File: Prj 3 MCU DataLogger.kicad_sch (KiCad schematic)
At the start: 25 parts, among them U1 24LC1025, U2 24LC1025, U3 DS1337S_, U4 ATMEGA328P-AU, Y1 Crystal, Y2 Crystal

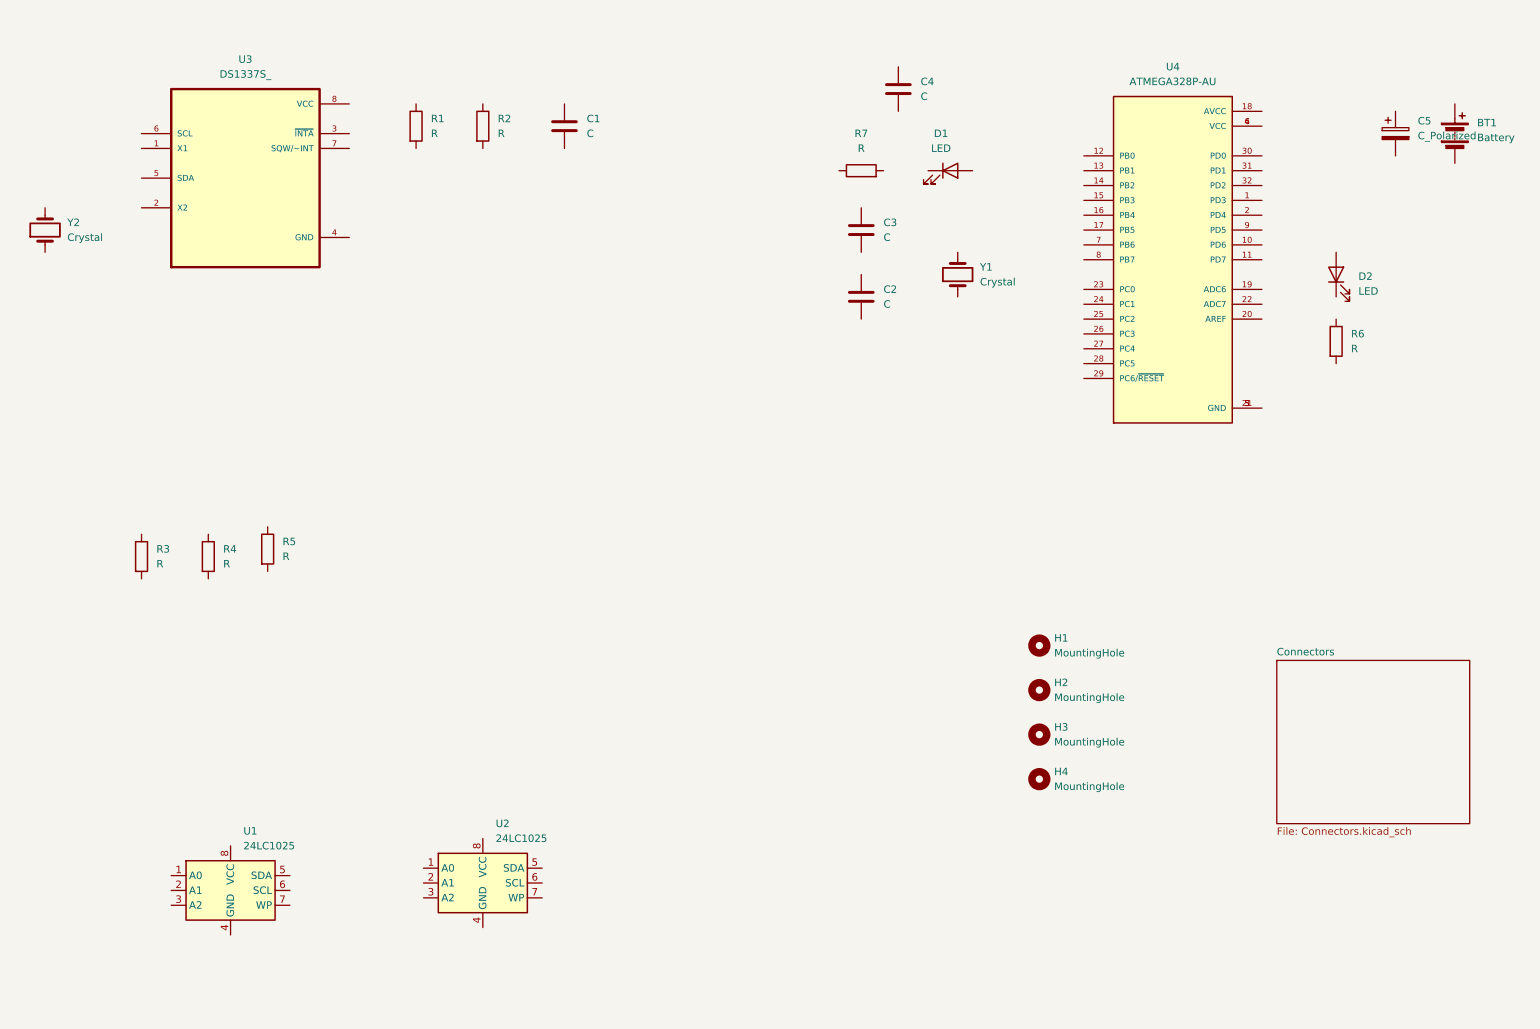
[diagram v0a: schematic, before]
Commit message: Component Values are added.
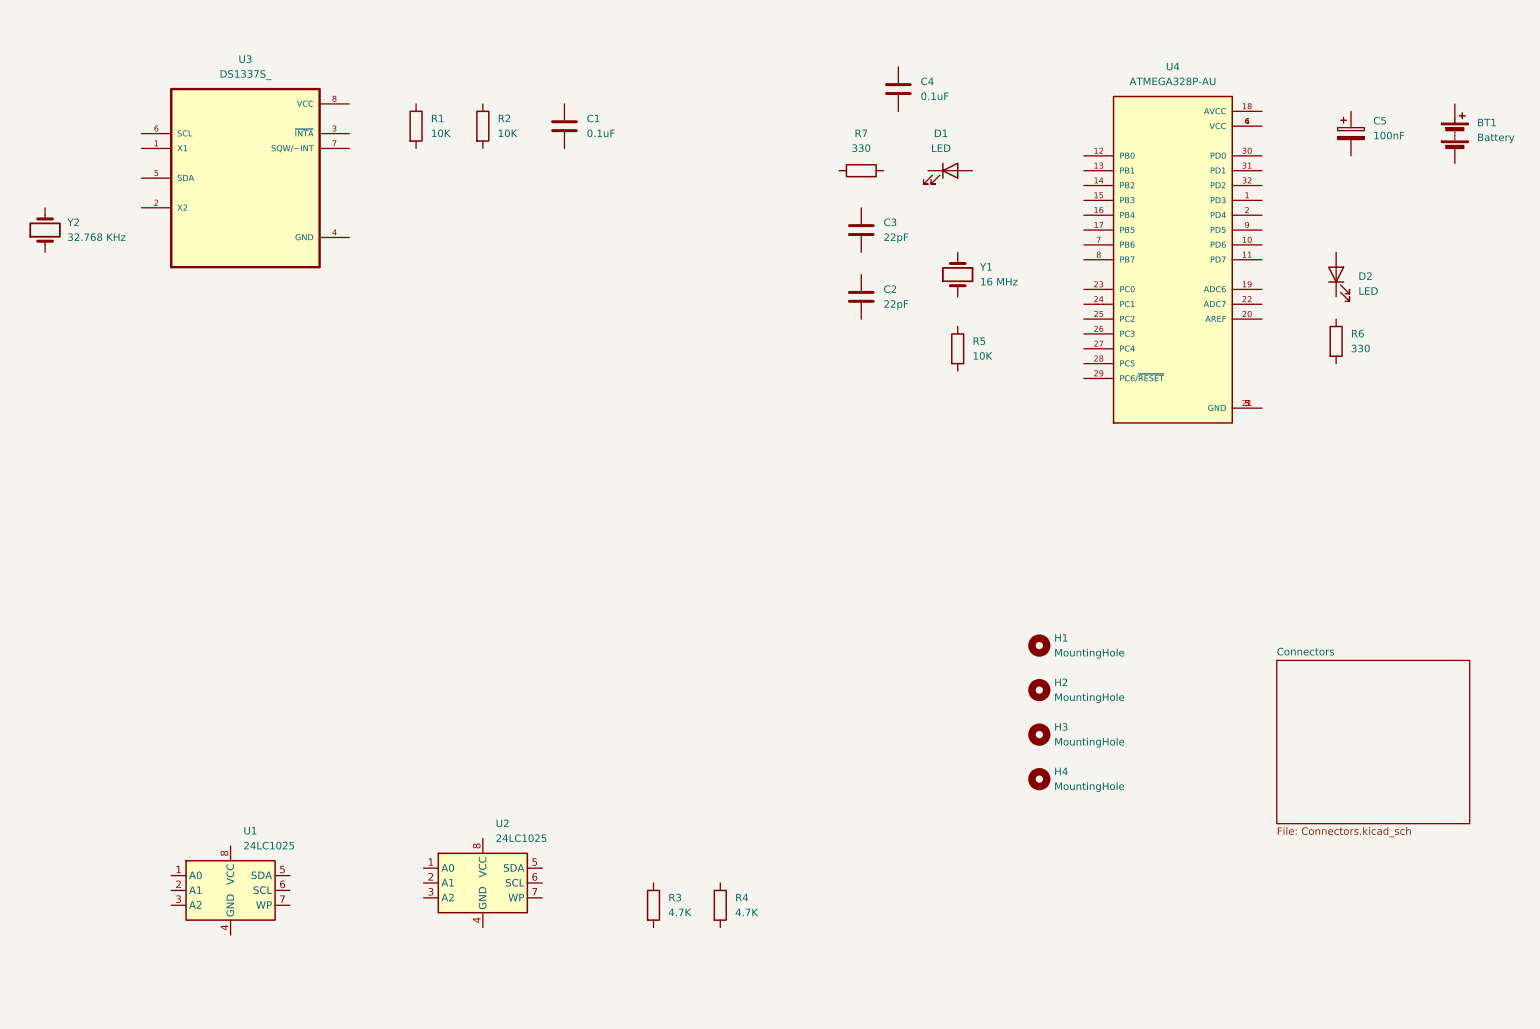
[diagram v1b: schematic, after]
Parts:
- C1, C4: value C -> 0.1uF
- C2, C3: value C -> 22pF
- C5: value C_Polarized -> 100nF
- R1, R2, R5: value R -> 10K
- R3, R4: value R -> 4.7K
- R6, R7: value R -> 330
- Y1: value Crystal -> 16 MHz
- Y2: value Crystal -> 32.768 KHz
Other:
- moved on the sheet: C5, R3, R4, R5

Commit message: Symbol to footprint associations are completed.
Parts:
- BT1: footprint (none) -> Connector_PinHeader_2.54mm:PinHeader_1x02_P2.54mm_Vertical
- C1, C2, C3, C4, C5: footprint (none) -> Capacitor_SMD:C_0805_2012Metric
- D1, D2: footprint (none) -> LED_SMD:LED_0805_2012Metric
- H1, H2, H3, H4: footprint (none) -> MountingHole:MountingHole_2.1mm
- R1, R2, R3, R4, R5, R6, R7: footprint (none) -> Resistor_SMD:R_0805_2012Metric
- U1, U2: footprint (none) -> Package_SO:SOIC-8_5.23x5.23mm_P1.27mm
- U3: footprint DS1337S_:SOIC127P600X175-8N -> MCU DataLogger Footprints:SOIC127P600X175-8N
- U4: footprint ATMEGA328P-AU:QFP80P900X900X120-32N -> MCU DataLogger Footprints:QFP80P900X900X120-32N
- Y1, Y2: footprint (none) -> Crystal:Crystal_SMD_5032-2Pin_5.0x3.2mm_HandSoldering
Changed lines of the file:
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@@
 			)
 		)
-		(property "Footprint" ""
+		(property "Footprint" "Resistor_SMD:R_0805_2012Metric"
 			(at 103.632 36.83 90)
 			(effects
@@
 			)
 		)
-		(property "Footprint" ""
+		(property "Footprint" "Capacitor_SMD:C_0805_2012Metric"
 			(at 120.3452 40.64 0)
 			(effects
@@
 			)
 		)
-		(property "Footprint" ""
+		(property "Footprint" "MountingHole:MountingHole_2.1mm"
 			(at 200.66 148.59 0)
 			(effects
@@
 			)
 		)
-		(property "Footprint" ""
+		(property "Footprint" "Resistor_SMD:R_0805_2012Metric"
 			(at 170.18 46.228 90)
 			(effects
@@
 			)
 		)
-		(property "Footprint" "DS1337S_:SOIC127P600X175-8N"
+		(property "Footprint" "MCU DataLogger Footprints:SOIC127P600X175-8N"
 			(at 64.77 45.72 0)
 			(effects
@@
 			)
 		)
-		(property "Footprint" ""
+		(property "Footprint" "MountingHole:MountingHole_2.1mm"
 			(at 200.66 125.73 0)
 			(effects
@@
 			)
 		)
-		(property "Footprint" ""
+		(property "Footprint" "MountingHole:MountingHole_2.1mm"
 			(at 200.66 140.97 0)
 			(effects
@@
 			)
 		)
-		(property "Footprint" ""
+		(property "Footprint" "Resistor_SMD:R_0805_2012Metric"
 			(at 184.912 74.93 90)
 			(effects
@@
 			)
 		)
-		(property "Footprint" ""
+		(property "Footprint" "Capacitor_SMD:C_0805_2012Metric"
 			(at 177.4952 34.29 0)
 			(effects
@@
 			)
 		)
-		(property "Footprint" "ATMEGA328P-AU:QFP80P900X900X120-32N"
+		(property "Footprint" "MCU DataLogger Footprints:QFP80P900X900X120-32N"
 			(at 223.52 59.69 0)
 			(effects
@@
 			)
 		)
-		(property "Footprint" ""
+		(property "Footprint" "LED_SMD:LED_0805_2012Metric"
 			(at 185.42 44.45 0)
 			(effects
@@
 			)
 		)
-		(property "Footprint" ""
+		(property "Footprint" "Crystal:Crystal_SMD_5032-2Pin_5.0x3.2mm_HandSoldering"
 			(at 30.48 54.61 0)
 			(effects
@@
 			)
 		)
-		(property "Footprint" ""
+		(property "Footprint" "LED_SMD:LED_0805_2012Metric"
 			(at 251.46 62.23 0)
 			(effects
@@
 			)
 		)
-		(property "Footprint" ""
+		(property "Footprint" "Resistor_SMD:R_0805_2012Metric"
 			(at 144.272 170.18 90)
 			(effects
@@
 			)
 		)
-		(property "Footprint" ""
+		(property "Footprint" "Crystal:Crystal_SMD_5032-2Pin_5.0x3.2mm_HandSoldering"
 			(at 186.69 62.23 0)
 			(effects
@@
 			)
 		)
-		(property "Footprint" ""
+		(property "Footprint" "Resistor_SMD:R_0805_2012Metric"
 			(at 92.202 36.83 90)
 			(effects
@@
 			)
 		)
-		(property "Footprint" ""
+		(property "Footprint" "Capacitor_SMD:C_0805_2012Metric"
 			(at 171.1452 58.42 0)
 			(effects
@@
 			)
 		)
-		(property "Footprint" ""
+		(property "Footprint" "Capacitor_SMD:C_0805_2012Metric"
 			(at 171.1452 69.85 0)
 			(effects
@@
 			)
 		)
-		(property "Footprint" ""
+		(property "Footprint" "Connector_PinHeader_2.54mm:PinHeader_1x02_P2.54mm_Vertical"
 			(at 271.78 36.576 90)
 			(effects
@@
 			)
 		)
-		(property "Footprint" ""
+		(property "Footprint" "Capacitor_SMD:C_0805_2012Metric"
 			(at 254.9652 41.91 0)
 			(effects
@@
 			)
 		)
-		(property "Footprint" ""
+		(property "Footprint" "Package_SO:SOIC-8_5.23x5.23mm_P1.27mm"
 			(at 105.41 166.37 0)
 			(effects
@@
 			)
 		)
-		(property "Footprint" ""
+		(property "Footprint" "Package_SO:SOIC-8_5.23x5.23mm_P1.27mm"
 			(at 62.23 167.64 0)
 			(effects
@@
 			)
 		)
-		(property "Footprint" ""
+		(property "Footprint" "Resistor_SMD:R_0805_2012Metric"
 			(at 132.842 170.18 90)
 			(effects
@@
 			)
 		)
-		(property "Footprint" ""
+		(property "Footprint" "MountingHole:MountingHole_2.1mm"
 			(at 200.66 133.35 0)
 			(effects
@@
 			)
 		)
-		(property "Footprint" ""
+		(property "Footprint" "Resistor_SMD:R_0805_2012Metric"
 			(at 249.682 73.66 90)
 			(effects

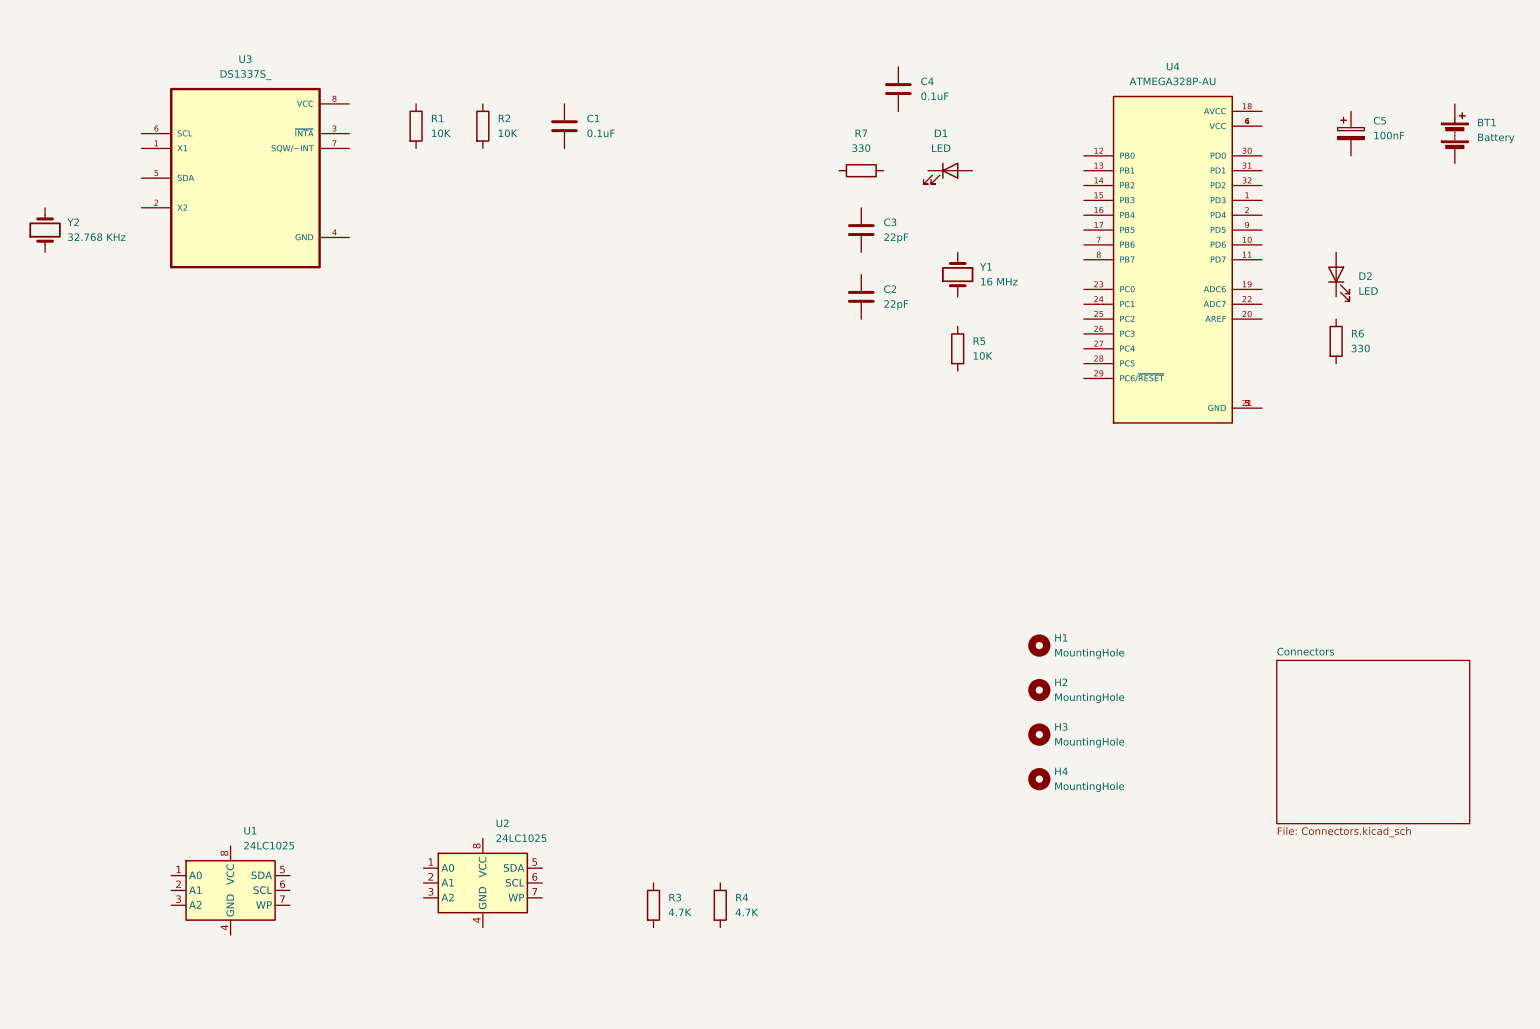
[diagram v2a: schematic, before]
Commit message: Wiring of the root sheet have been completed.
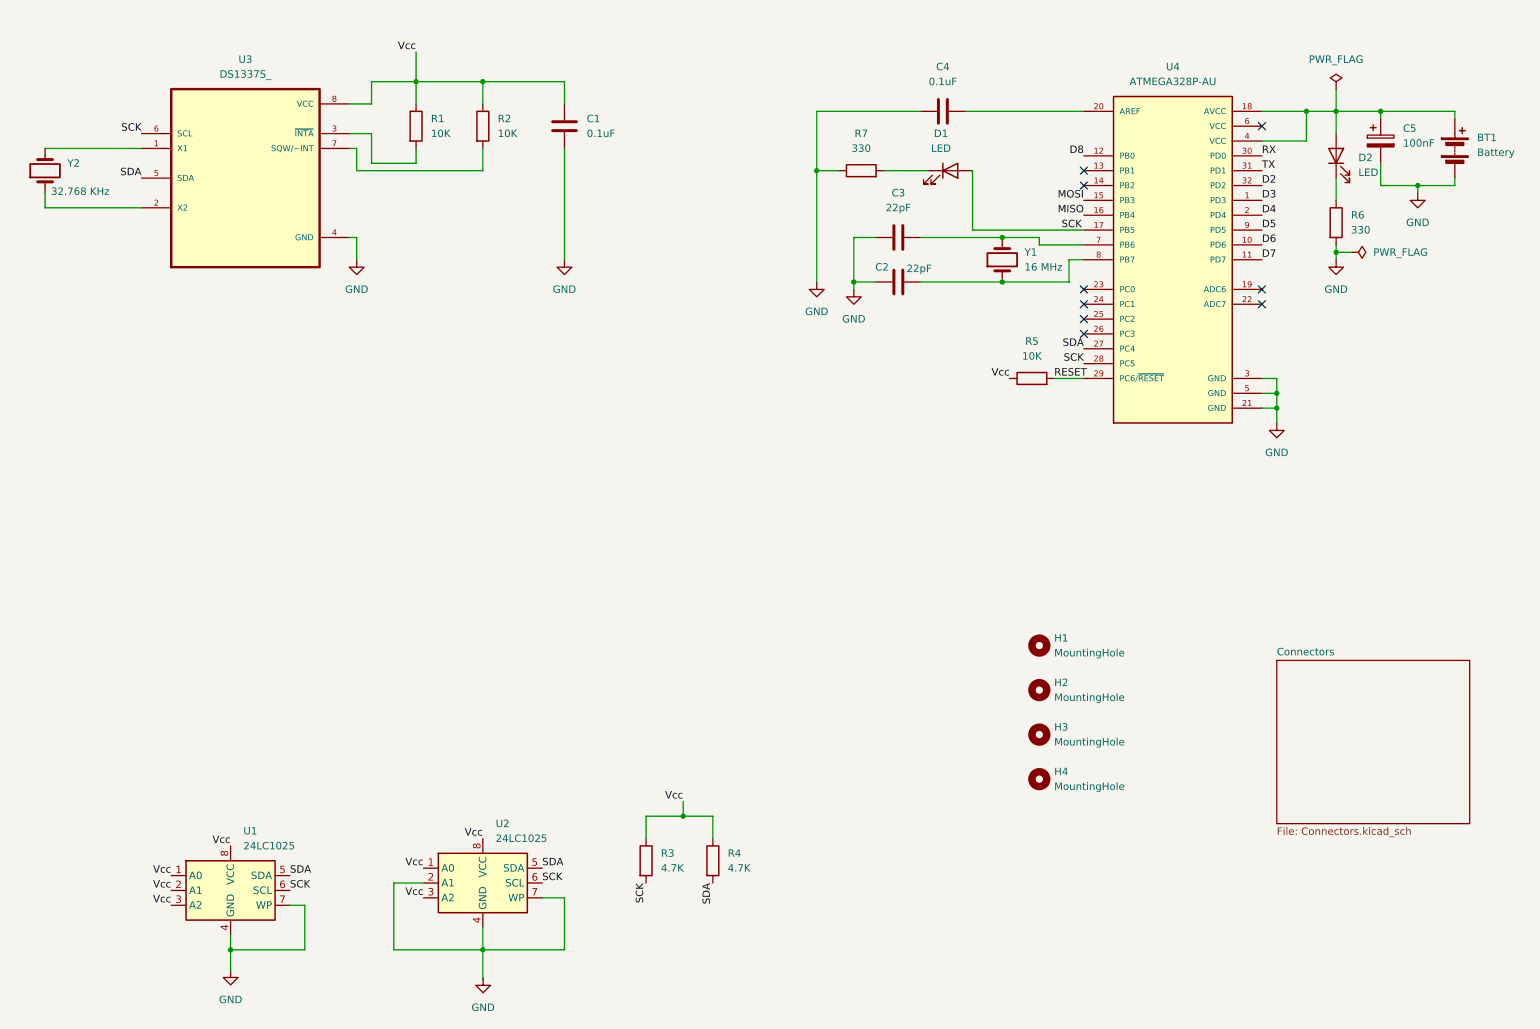
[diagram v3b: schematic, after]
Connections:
- net Vcc: now reaches R2.1
- net Vcc: now also C1.1, R1.1, R3.1, R4.1, R5.1, U1.1 (A0), U1.2 (A1), U1.3 (A2), U1.8 (VCC), U2.1 (A0), U2.3 (A2), U2.8 (VCC), U3.8 (VCC)
- net at R2.2: now also U3.7 (SQW/~INT)
- net GND: now reaches C1.2
- net GND: now also BT1.2 (-), C2.1, C3.1, C4.1, C5.2, R6.2, R7.1, U3.4 (GND), U4.21 (GND), U4.3 (GND), U4.5 (GND)
- net at R7.2: now also D1.1 (K)
- net at U3.1 (X1): now also Y2.2
- net at U3.2 (X2): now also Y2.1
- net at U3.3 (~{INTA}): now also R1.2
- net SDA: now reaches U3.5 (SDA)
- net SDA: now also R4.2, U1.5 (SDA), U2.5 (SDA), U4.27 (PC4)
- net SCK: now reaches U3.6 (SCL)
- net SCK: now also D1.2 (A), R3.2, U1.6 (SCL), U2.6 (SCL), U4.17 (PB5), U4.28 (PC5)
- net RESET: now reaches R5.2
- net RESET: now also U4.29 (PC6/~{RESET})
- net at C4.2: now also U4.20 (AREF)
- net D3: now reaches U4.1 (PD3)
- net D6: now reaches U4.10 (PD6)
- net D7: now reaches U4.11 (PD7)
- net D8: now reaches U4.12 (PB0)
- net MOSI: now reaches U4.15 (PB3)
- net MISO: now reaches U4.16 (PB4)
- net at U4.18 (AVCC): now also BT1.1 (+), C5.1, D2.2 (A), U4.4 (VCC)
- net D4: now reaches U4.2 (PD4)
- net RX: now reaches U4.30 (PD0)
- net TX: now reaches U4.31 (PD1)
- net D2: now reaches U4.32 (PD2)
- net at U4.6 (VCC): no longer U4.4 (VCC)
- net at U4.7 (PB6): now also C3.2, Y1.2
- net at U4.8 (PB7): now also C2.2, Y1.1
- net D5: now reaches U4.9 (PD5)
- net at D2.1 (K): now also R6.1
- net at U2.2 (A1): now also U2.4 (GND), U2.7 (WP)
- net at U1.4 (GND): now also U1.7 (WP)
- no-connect marks 0 -> 9
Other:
- company: (none) -> Tech Exploration / Dr. Peter Dalmaris
- moved on the sheet: BT1, C2, C3, C4, C5, D2, R3, R4, R5, R6, Y1, Y2

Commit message: Second sheets connections are done.
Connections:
- net GND: now also U1.4 (GND), U1.7 (WP), U2.2 (A1), U2.4 (GND), U2.7 (WP)
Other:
- sheet Connectors ports: added D2, D3, D4, D5, D6, D7, D8, GND, MISO, MOSI, RESET, RX, SCK, SDA, TX, Vcc; removed none
- moved on the sheet: H1, H2, H3, H4

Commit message: Comments completed.
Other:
- note added: "EEPROM"
- note added: "MCU"
- note added: "Real Time Clock"
- moved on the sheet: BT1, C1, C2, C3, C4, C5, D1, D2, R1, R2, R3, R4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

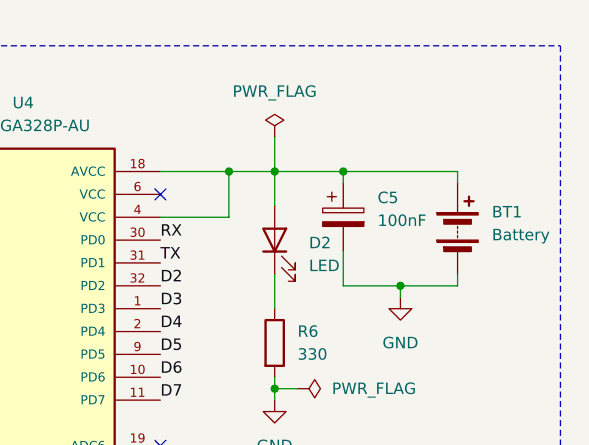
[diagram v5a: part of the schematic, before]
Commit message: Fixed all DRC errors and F&B Silkscreens completed.
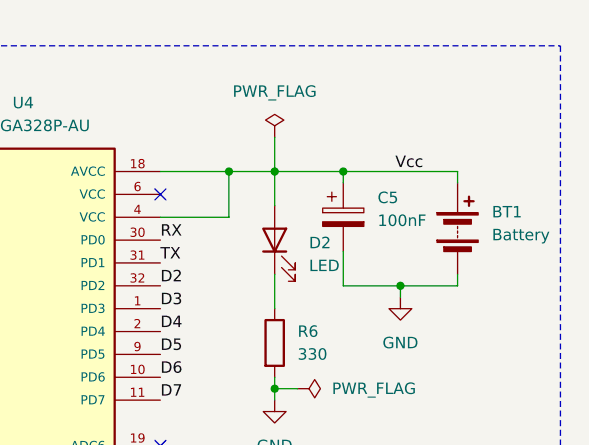
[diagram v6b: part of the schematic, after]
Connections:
- net Vcc: now also BT1.1 (+), C5.1, D2.2 (A), U4.18 (AVCC), U4.4 (VCC)
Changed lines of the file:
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@@
+		)
+	)
+	(label "Vcc"
+		(at 259.08 34.29 180)
+		(fields_autoplaced yes)
+		(effects
+			(font
+				(size 1.27 1.27)
+			)
+			(justify right bottom)
 		)
 	)
